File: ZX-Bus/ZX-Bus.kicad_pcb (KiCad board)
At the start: 2 copper layers, 126.9 x 142.3 mm, 40 parts, among them J1 DIP-40 Pins, J2 Conn_01x04_Pin, J3 Conn_01x08_Pin, J4 Power, J5 Main board power, J6 12V, J7 5V, J8 Reset, U1 Z84C00xxP, U2 74LS245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

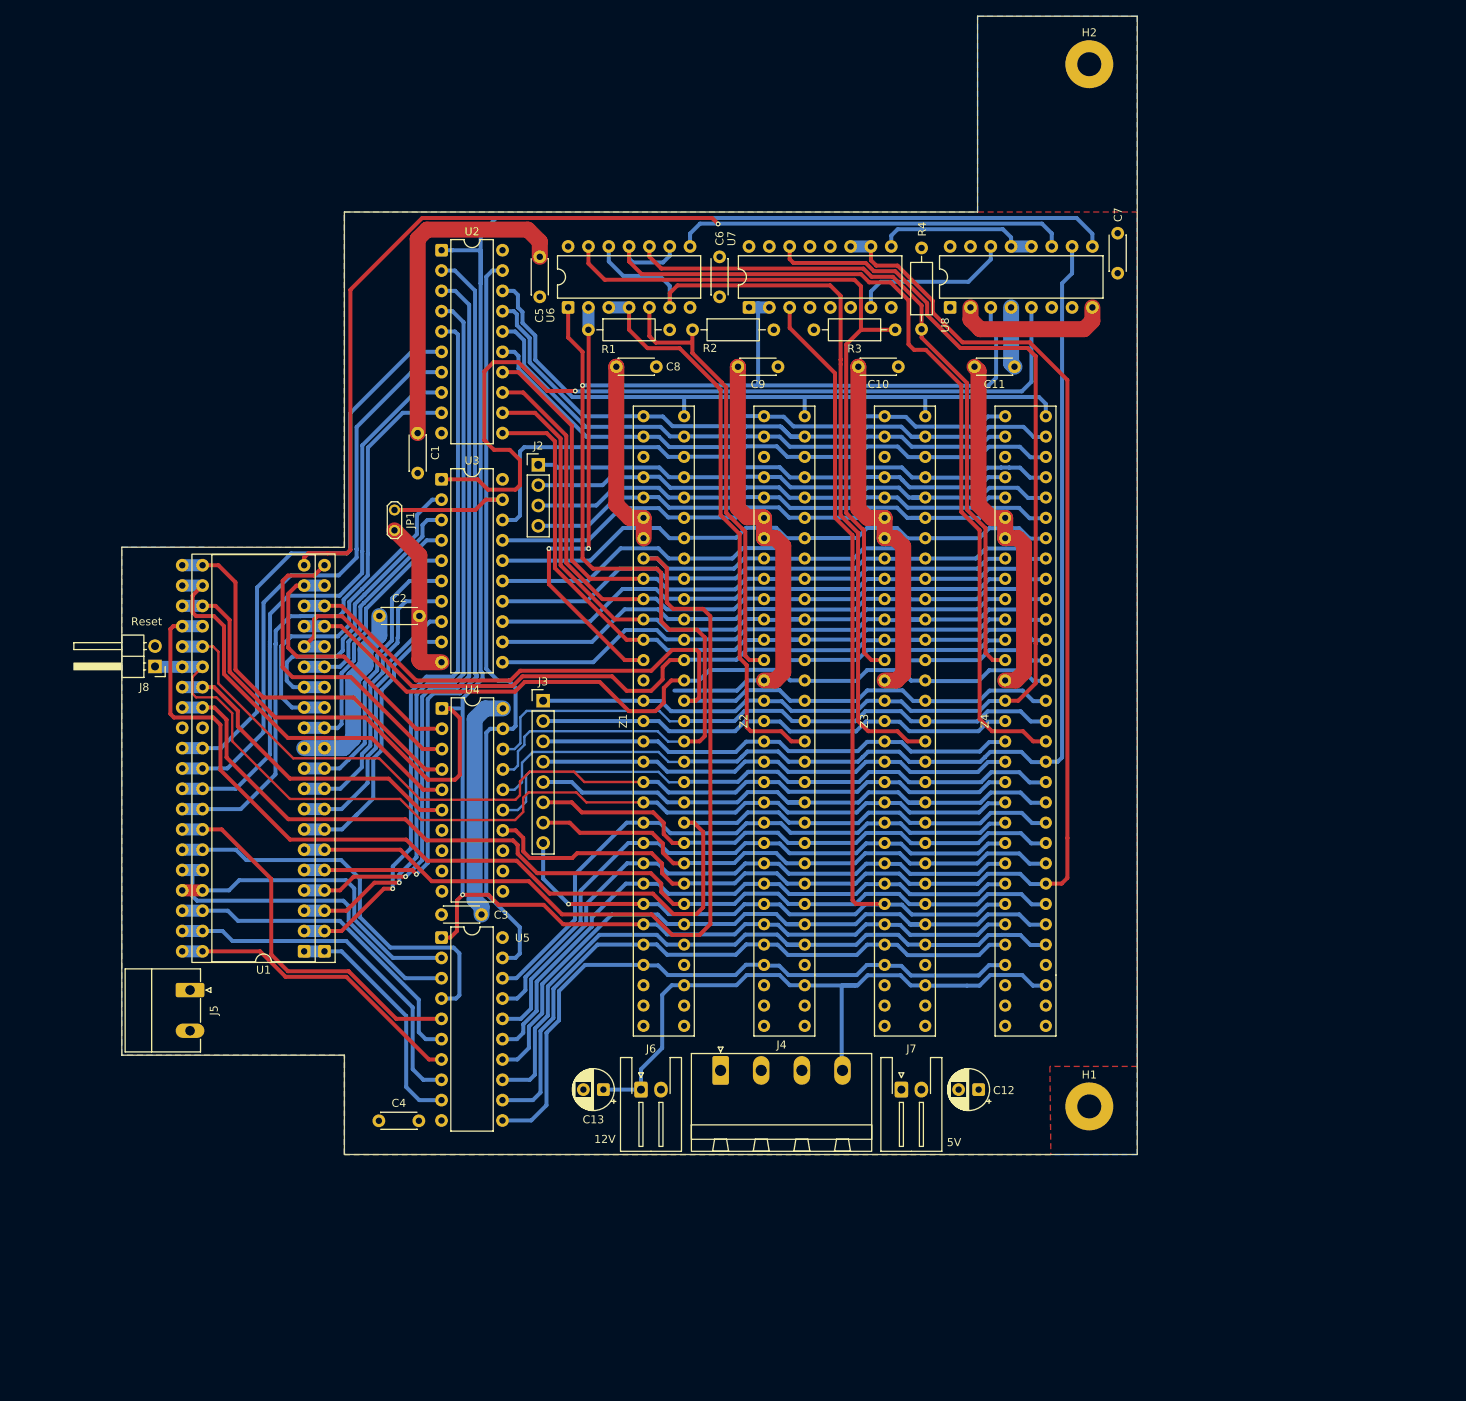
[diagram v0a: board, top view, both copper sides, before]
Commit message: ZX-Bus: Proper sides on NemoBus slots
Fix swapped A and B rows
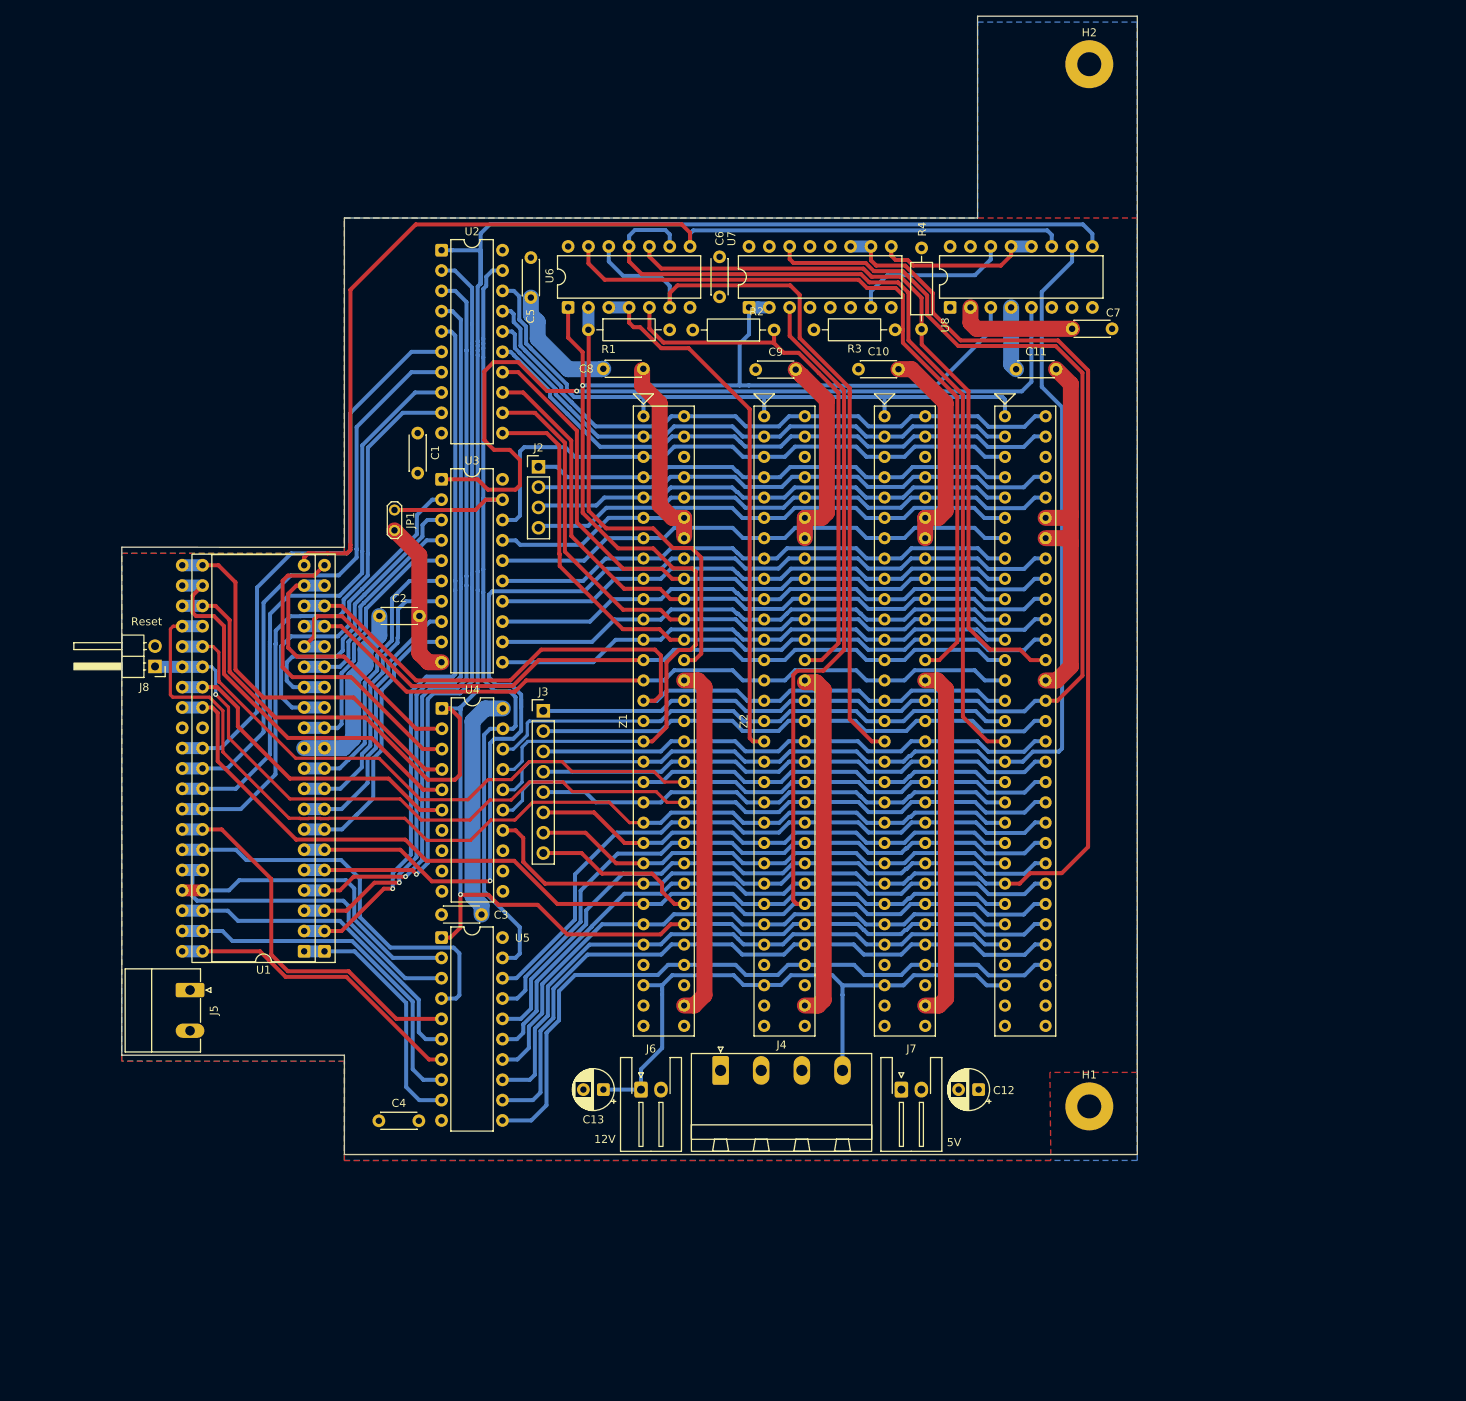
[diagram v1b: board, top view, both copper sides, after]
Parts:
- moved C7 12.0 mm to (150.5, 70.0), turned to 180 degrees
- moved R2 10.2 mm to (108.3, 70.1), turned to 180 degrees
- moved C8 6.63 mm to (86.9, 75.0), turned to 0 degrees
- moved C10 4.99 mm to (118.8, 75.0), turned to 0 degrees
- moved C9 2.81 mm to (106.0, 75.0), turned to 0 degrees
- moved J3 1.26 mm to (79.4, 117.7)
- moved C5 1.12 mm to (77.9, 66.0)
- moved C11 0.37 mm to (138.5, 75.0), turned to 0 degrees
- moved J2 0.24 mm to (78.8, 87.2)
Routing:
- net GND: track 254.2 -> 292.4 mm
- net /~{WAIT}: track 156.0 -> 133.6 mm
- net VCC: track 59.8 -> 75.7 mm
- net /~{RDR}: track 142.8 -> 155.8 mm
- net /CLK: track 154.6 -> 142.0 mm, vias 0 -> 1
- net Net-(Z2-~{IORQGE}): track 55.4 -> 67.6 mm
- net /D4: track 79.2 -> 67.1 mm
- net /~{IORQ}: track 170.5 -> 158.7 mm
- net /A13: track 83.5 -> 72.8 mm
- net /A8: track 87.0 -> 76.7 mm
- net /D3: track 77.3 -> 67.1 mm
- net /~{IODOS}: track 71.2 -> 61.4 mm
- net /~{NMI}: track 104.0 -> 94.7 mm
- net /TURBO: track 69.9 -> 61.5 mm
- net /A10: track 86.9 -> 78.5 mm
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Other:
- outline, holes or cut-outs redrawn
- board text removed: "NemoBus"

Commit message: ZX-Bus: Complete v1
Add missing parts and complete layout
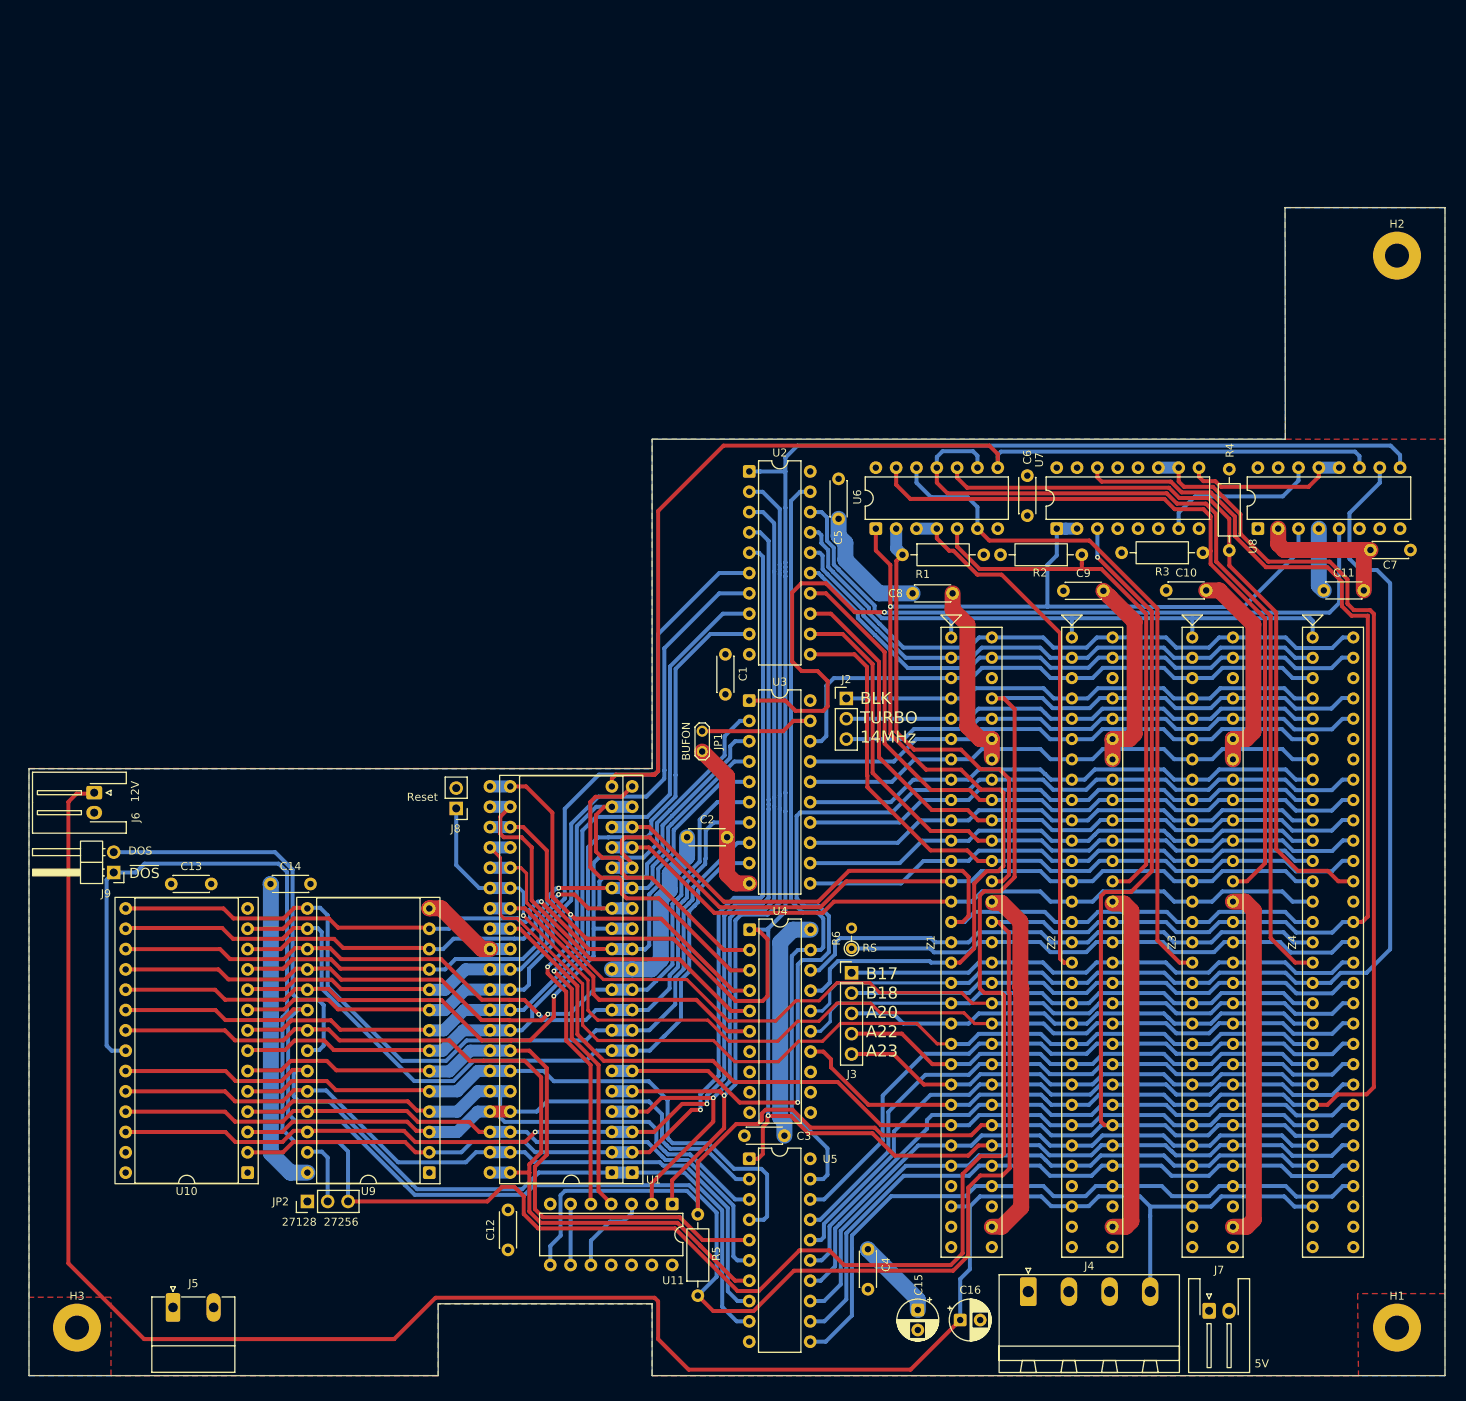
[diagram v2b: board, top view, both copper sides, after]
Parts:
- added C14: 0.1uF, Capacitor_THT:C_Disc_D4.3mm_W1.9mm_P5.00mm, F.Cu at (45.3, 139.3)
- added C15: 220uF, Capacitor_THT:CP_Radial_D5.0mm_P2.50mm, F.Cu at (126.3, 192.6)
- added C16: 220uF, Capacitor_THT:CP_Radial_D5.0mm_P2.50mm, F.Cu at (131.6, 193.9)
- added H3: MountingHole 3mm, MountingHole:MountingHole_3mm_Pad, F.Cu at (21.2, 194.8)
- added J9: PLS-2R, Connector_PinHeader_2.54mm:PinHeader_1x02_P2.54mm_Horizontal, F.Cu at (25.7, 137.9)
- added JP2: ROM type, Connector_PinHeader_2.54mm:PinHeader_1x03_P2.54mm_Vertical, F.Cu at (49.9, 179.0)
- added R5: 510, Resistor_THT:R_Axial_DIN0207_L6.3mm_D2.5mm_P10.16mm_Horizontal, F.Cu at (98.8, 190.8)
- added R6: 10K, Resistor_THT:R_Axial_DIN0204_L3.6mm_D1.6mm_P2.54mm_Vertical, F.Cu at (118.0, 147.4)
- added U10: 27128, Package_DIP:DIP-28_W15.24mm_Socket, F.Cu at (42.5, 175.4)
- added U11: 74ALS1032, Package_DIP:DIP-14_W7.62mm, F.Cu at (95.6, 179.4)
- added U9: 27128, Package_DIP:DIP-28_W15.24mm_Socket, F.Cu at (65.2, 175.4)
- C12, C13: value 220uF -> 0.1uF; footprint Capacitor_THT:CP_Radial_D5.0mm_P2.50mm -> Capacitor_THT:C_Disc_D4.3mm_W1.9mm_P5.00mm
- J2: value Conn_01x04_Pin -> PLS-3; footprint Connector_PinHeader_2.54mm:PinHeader_1x04_P2.54mm_Vertical -> Connector_PinHeader_2.54mm:PinHeader_1x03_P2.54mm_Vertical
- J3: value Conn_01x08_Pin -> PLS-6; footprint Connector_PinHeader_2.54mm:PinHeader_1x08_P2.54mm_Vertical -> Connector_PinHeader_2.54mm:PinHeader_1x05_P2.54mm_Vertical
- J8: footprint Connector_PinHeader_2.54mm:PinHeader_1x02_P2.54mm_Horizontal -> Connector_PinHeader_2.54mm:PinHeader_1x02_P2.54mm_Vertical
- moved J6 77.8 mm to (23.3, 127.9), turned to -90 degrees
- moved C4 63.2 mm to (120.0, 185.0), turned to -90 degrees
- moved C12 62.1 mm to (75.0, 185.1), turned to 90 degrees
- moved C13 59.8 mm to (32.9, 139.3), turned to 0 degrees
- moved J3 50.6 mm to (118.0, 150.4)
- moved R1 48.3 mm to (124.3, 98.2)
- moved J2 48.2 mm to (117.3, 116.2)
- moved C8 47.8 mm to (125.6, 103.0)
- moved R2 47.6 mm to (146.8, 98.2)
- moved R3 47.5 mm to (161.9, 97.9)
- moved C10 47.4 mm to (157.3, 102.7)
- moved C2 47.4 mm to (97.4, 133.5)
- moved C9 47.4 mm to (144.5, 102.7)
- moved J1 47.4 mm to (88.0, 175.4)
- moved U1 47.4 mm to (90.6, 175.4)
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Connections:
- C13 pad 1: +12V -> VCC
- J2 pad 2: /~{DOS} -> /TURBO
- J2 pad 3: /TURBO -> /F
- J3 pad 1: /~{RDR} -> /B17
- J3 pad 2: /RS -> /B18
- J3 pad 3: /B17 -> /A20
- J3 pad 4: /B18 -> /A22
- J3 pad 5: /~{IODOS} -> /A23
- Z1 pad A20: /~{IODOS} -> /A20
- Z2 pad A20: /~{IODOS} -> /A20
- Z3 pad A20: /~{IODOS} -> /A20
- Z4 pad A20: /~{IODOS} -> /A20
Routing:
- net /~{DOS}: track 66.9 -> 311.8 mm
- net +12V: track 77.8 -> 261.4 mm
- net /~{RDR}: track 155.8 -> 327.3 mm
- net /*D3: track 34.1 -> 110.7 mm
- net /*D4: track 35.1 -> 110.5 mm
- net /*A11: track 31.0 -> 105.9 mm
- net /*D7: track 43.0 -> 114.4 mm, vias 0 -> 1
- net /*A10: track 38.0 -> 109.0 mm
- net /*D5: track 35.8 -> 102.0 mm, vias 0 -> 1
- net /*D6: track 35.5 -> 101.6 mm, vias 0 -> 1
- net /*A13: track 91.7 -> 154.7 mm, vias 1 -> 2
- net /~{IODOS}: track 61.4 -> 0.00 mm
- net /A20: track 0.00 -> 61.4 mm
- net /*~{MREQ}: track 35.1 -> 91.4 mm, vias 0 -> 1
- net /~{CSROM}: track 152.2 -> 208.5 mm, vias 0 -> 1
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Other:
- board size 126.9 x 142.3 mm -> 177 x 146 mm
- board text added: "27128 27256"
- board text added: "B17 B18 A20 A22 A23"
- board text added: "BLK TURBO 14MHz"
- board text added: "DOS"
- board text added: "RS"
- board text added: "~{DOS}"
